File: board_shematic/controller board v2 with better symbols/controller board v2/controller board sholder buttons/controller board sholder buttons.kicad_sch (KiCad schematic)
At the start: 6 parts, among them J1 Conn_01x03_Pin, J2 Conn_01x03_Pin, SW1 SW_Push, SW2 SW_Push, SW3 SW_Push, SW4 SW_Push

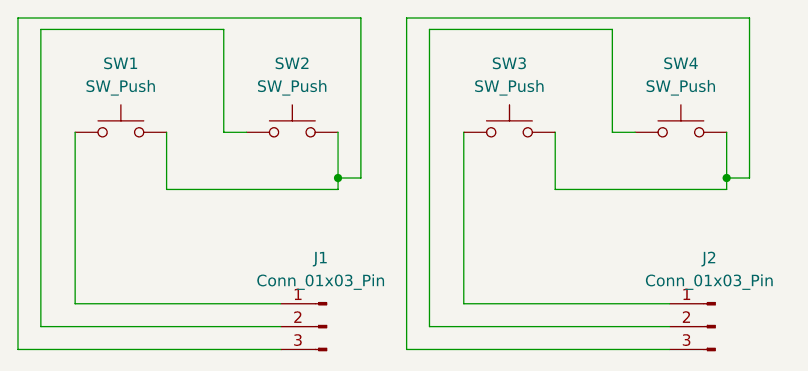
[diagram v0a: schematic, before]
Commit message: changed hole locations, updated pin orientation
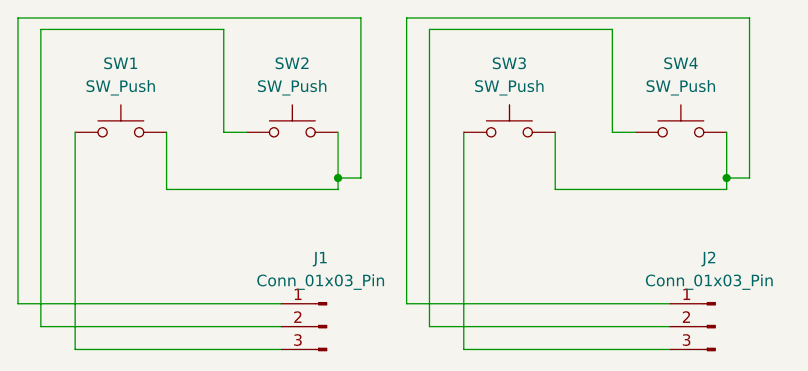
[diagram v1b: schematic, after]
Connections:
- net at J1.1 (Pin_1): now also SW1.2, SW2.2; no longer SW1.1
- net at SW3.2, SW4.2: now also J2.1 (Pin_1); no longer J2.3 (Pin_3)
- net at SW3.1: now also J2.3 (Pin_3); no longer J2.1 (Pin_1)
- new net: J1.3 (Pin_3), SW1.1
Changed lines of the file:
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@@
   (junction (at 134.62 74.93) (diameter 0) (color 0 0 0 0)
   )
+  (wire (pts (xy 134.62 74.93) (xy 137.16 74.93))
+    (stroke (width 0) (type default))
+  )
+  (wire (pts (xy 148.59 69.85) (xy 148.59 93.98))
+    (stroke (width 0) (type default))
+  )
+  (wire (pts (xy 165.1 58.42) (xy 165.1 69.85))
+    (stroke (width 0) (type default))
+  )
+  (wire (pts (xy 105.41 69.85) (xy 105.41 93.98))
+    (stroke (width 0) (type default))
+  )
+  (wire (pts (xy 142.24 57.15) (xy 142.24 88.9))
+    (stroke (width 0) (type default))
+  )
+  (wire (pts (xy 134.62 76.2) (xy 134.62 74.93))
+    (stroke (width 0) (type default))
+  )
+  (wire (pts (xy 142.24 57.15) (xy 180.34 57.15))
+    (stroke (width 0) (type default))
+  )
+  (wire (pts (xy 99.06 57.15) (xy 99.06 88.9))
+    (stroke (width 0) (type default))
+  )
+  (wire (pts (xy 177.8 74.93) (xy 177.8 69.85))
+    (stroke (width 0) (type default))
+  )
+  (wire (pts (xy 158.75 76.2) (xy 177.8 76.2))
+    (stroke (width 0) (type default))
+  )
+  (wire (pts (xy 137.16 57.15) (xy 137.16 74.93))
+    (stroke (width 0) (type default))
+  )
+  (wire (pts (xy 158.75 69.85) (xy 158.75 76.2))
+    (stroke (width 0) (type default))
+  )
+  (wire (pts (xy 99.06 57.15) (xy 137.16 57.15))
+    (stroke (width 0) (type default))
+  )
+  (wire (pts (xy 148.59 93.98) (xy 171.45 93.98))
+    (stroke (width 0) (type default))
+  )
+  (wire (pts (xy 101.6 58.42) (xy 121.92 58.42))
+    (stroke (width 0) (type default))
+  )
+  (wire (pts (xy 180.34 57.15) (xy 180.34 74.93))
+    (stroke (width 0) (type default))
+  )
+  (wire (pts (xy 171.45 91.44) (xy 144.78 91.44))
+    (stroke (width 0) (type default))
+  )
+  (wire (pts (xy 177.8 74.93) (xy 180.34 74.93))
+    (stroke (width 0) (type default))
+  )
+  (wire (pts (xy 121.92 69.85) (xy 124.46 69.85))
+    (stroke (width 0) (type default))
+  )
+  (wire (pts (xy 165.1 69.85) (xy 167.64 69.85))
+    (stroke (width 0) (type default))
+  )
   (wire (pts (xy 177.8 76.2) (xy 177.8 74.93))
     (stroke (width 0) (type default))
   )
-  (wire (pts (xy 134.62 74.93) (xy 137.16 74.93))
-    (stroke (width 0) (type default))
-  )
-  (wire (pts (xy 105.41 88.9) (xy 105.41 69.85))
-    (stroke (width 0) (type default))
-  )
-  (wire (pts (xy 171.45 91.44) (xy 144.78 91.44))
-    (stroke (width 0) (type default))
-  )
-  (wire (pts (xy 134.62 76.2) (xy 134.62 74.93))
-    (stroke (width 0) (type default))
-  )
-  (wire (pts (xy 99.06 93.98) (xy 99.06 57.15))
-    (stroke (width 0) (type default))
-  )
-  (wire (pts (xy 137.16 57.15) (xy 137.16 74.93))
-    (stroke (width 0) (type default))
-  )
-  (wire (pts (xy 177.8 74.93) (xy 177.8 69.85))
-    (stroke (width 0) (type default))
-  )
-  (wire (pts (xy 142.24 93.98) (xy 142.24 57.15))
-    (stroke (width 0) (type default))
-  )
-  (wire (pts (xy 99.06 57.15) (xy 137.16 57.15))
-    (stroke (width 0) (type default))
-  )
-  (wire (pts (xy 171.45 93.98) (xy 142.24 93.98))
-    (stroke (width 0) (type default))
-  )
-  (wire (pts (xy 101.6 58.42) (xy 121.92 58.42))
-    (stroke (width 0) (type default))
-  )
-  (wire (pts (xy 148.59 88.9) (xy 148.59 69.85))
-    (stroke (width 0) (type default))
-  )
-  (wire (pts (xy 121.92 69.85) (xy 124.46 69.85))
-    (stroke (width 0) (type default))
-  )
-  (wire (pts (xy 165.1 69.85) (xy 167.64 69.85))
-    (stroke (width 0) (type default))
-  )
-  (wire (pts (xy 165.1 58.42) (xy 165.1 69.85))
-    (stroke (width 0) (type default))
-  )
-  (wire (pts (xy 158.75 69.85) (xy 158.75 76.2))
+  (wire (pts (xy 105.41 93.98) (xy 128.27 93.98))
+    (stroke (width 0) (type default))
+  )
+  (wire (pts (xy 134.62 74.93) (xy 134.62 69.85))
+    (stroke (width 0) (type default))
+  )
+  (wire (pts (xy 128.27 91.44) (xy 101.6 91.44))
+    (stroke (width 0) (type default))
+  )
+  (wire (pts (xy 142.24 88.9) (xy 171.45 88.9))
+    (stroke (width 0) (type default))
+  )
+  (wire (pts (xy 115.57 69.85) (xy 115.57 76.2))
+    (stroke (width 0) (type default))
+  )
+  (wire (pts (xy 99.06 88.9) (xy 128.27 88.9))
+    (stroke (width 0) (type default))
+  )
+  (wire (pts (xy 101.6 91.44) (xy 101.6 58.42))
+    (stroke (width 0) (type default))
+  )
+  (wire (pts (xy 115.57 76.2) (xy 134.62 76.2))
+    (stroke (width 0) (type default))
+  )
+  (wire (pts (xy 121.92 58.42) (xy 121.92 69.85))
+    (stroke (width 0) (type default))
+  )
+  (wire (pts (xy 144.78 58.42) (xy 165.1 58.42))
     (stroke (width 0) (type default))
   )
@@
     (stroke (width 0) (type default))
   )
-  (wire (pts (xy 134.62 74.93) (xy 134.62 69.85))
-    (stroke (width 0) (type default))
-  )
-  (wire (pts (xy 128.27 91.44) (xy 101.6 91.44))
-    (stroke (width 0) (type default))
-  )
-  (wire (pts (xy 177.8 74.93) (xy 180.34 74.93))
-    (stroke (width 0) (type default))
-  )
-  (wire (pts (xy 144.78 58.42) (xy 165.1 58.42))
-    (stroke (width 0) (type default))
-  )
-  (wire (pts (xy 115.57 69.85) (xy 115.57 76.2))
-    (stroke (width 0) (type default))
-  )
-  (wire (pts (xy 142.24 57.15) (xy 180.34 57.15))
-    (stroke (width 0) (type default))
-  )
-  (wire (pts (xy 180.34 57.15) (xy 180.34 74.93))
-    (stroke (width 0) (type default))
-  )
-  (wire (pts (xy 128.27 88.9) (xy 105.41 88.9))
-    (stroke (width 0) (type default))
-  )
-  (wire (pts (xy 171.45 88.9) (xy 148.59 88.9))
-    (stroke (width 0) (type default))
-  )
-  (wire (pts (xy 101.6 91.44) (xy 101.6 58.42))
-    (stroke (width 0) (type default))
-  )
-  (wire (pts (xy 128.27 93.98) (xy 99.06 93.98))
-    (stroke (width 0) (type default))
-  )
-  (wire (pts (xy 115.57 76.2) (xy 134.62 76.2))
-    (stroke (width 0) (type default))
-  )
-  (wire (pts (xy 158.75 76.2) (xy 177.8 76.2))
-    (stroke (width 0) (type default))
-  )
-  (wire (pts (xy 121.92 58.42) (xy 121.92 69.85))
-    (stroke (width 0) (type default))
+  (symbol (lib_id "Switch:SW_Push") (at 153.67 69.85 0) (unit 1)
+    (in_bom yes) (on_board yes) (dnp no) (fields_autoplaced)
+    (property "Reference" "SW3" (at 153.67 62.23 0)
+      (effects (font (size 1.27 1.27)))
+    )
+    (property "Value" "SW_Push" (at 153.67 64.77 0)
+      (effects (font (size 1.27 1.27)))
+    )
+    (property "Footprint" "Button_Switch_THT:SW_PUSH_6mm_H5mm" (at 153.67 64.77 0)
+      (effects (font (size 1.27 1.27)) hide)
+    )
+    (property "Datasheet" "~" (at 153.67 64.77 0)
+      (effects (font (size 1.27 1.27)) hide)
+    )
+    (pin "2")
+    (pin "1")
+    (instances
+      (project "controller board sholder buttons"
+        (path "/e512c459-defe-42ca-9db2-2e1aa3ed270f"
+          (reference "SW3") (unit 1)
+        )
+      )
+    )
   )
   (symbol (lib_id "Connector:Conn_01x03_Pin") (at 133.35 91.44 0) (mirror y) (unit 1)
@@
     )
   )
-  (symbol (lib_id "Switch:SW_Push") (at 172.72 69.85 0) (unit 1)
-    (in_bom yes) (on_board yes) (dnp no) (fields_autoplaced)
-    (property "Reference" "SW4" (at 172.72 62.23 0)
-      (effects (font (size 1.27 1.27)))
-    )
-    (property "Value" "SW_Push" (at 172.72 64.77 0)
-      (effects (font (size 1.27 1.27)))
-    )
-    (property "Footprint" "Button_Switch_THT:SW_PUSH_6mm_H5mm" (at 172.72 64.77 0)
-      (effects (font (size 1.27 1.27)) hide)
-    )
-    (property "Datasheet" "~" (at 172.72 64.77 0)
-      (effects (font (size 1.27 1.27)) hide)
-    )
-    (pin "2")
-    (pin "1")
-    (instances
-      (project "controller board sholder buttons"
-        (path "/e512c459-defe-42ca-9db2-2e1aa3ed270f"
-          (reference "SW4") (unit 1)
-        )
-      )
-    )
-  )
   (symbol (lib_id "Switch:SW_Push") (at 129.54 69.85 0) (unit 1)
     (in_bom yes) (on_board yes) (dnp no) (fields_autoplaced)
@@
     )
   )
-  (symbol (lib_id "Switch:SW_Push") (at 153.67 69.85 0) (unit 1)
-    (in_bom yes) (on_board yes) (dnp no) (fields_autoplaced)
-    (property "Reference" "SW3" (at 153.67 62.23 0)
-      (effects (font (size 1.27 1.27)))
-    )
-    (property "Value" "SW_Push" (at 153.67 64.77 0)
-      (effects (font (size 1.27 1.27)))
-    )
-    (property "Footprint" "Button_Switch_THT:SW_PUSH_6mm_H5mm" (at 153.67 64.77 0)
-      (effects (font (size 1.27 1.27)) hide)
-    )
-    (property "Datasheet" "~" (at 153.67 64.77 0)
-      (effects (font (size 1.27 1.27)) hide)
-    )
-    (pin "2")
-    (pin "1")
-    (instances
-      (project "controller board sholder buttons"
-        (path "/e512c459-defe-42ca-9db2-2e1aa3ed270f"
-          (reference "SW3") (unit 1)
-        )
-      )
+  (symbol (lib_id "Switch:SW_Push") (at 172.72 69.85 0) (unit 1)
+    (in_bom yes) (on_board yes) (dnp no) (fields_autoplaced)
+    (property "Reference" "SW4" (at 172.72 62.23 0)
+      (effects (font (size 1.27 1.27)))
+    )
+    (property "Value" "SW_Push" (at 172.72 64.77 0)
+      (effects (font (size 1.27 1.27)))
+    )
+    (property "Footprint" "Button_Switch_THT:SW_PUSH_6mm_H5mm" (at 172.72 64.77 0)
+      (effects (font (size 1.27 1.27)) hide)
+    )
+    (property "Datasheet" "~" (at 172.72 64.77 0)
+      (effects (font (size 1.27 1.27)) hide)
+    )
+    (pin "2")
+    (pin "1")
+    (instances
+      (project "controller board sholder buttons"
+        (path "/e512c459-defe-42ca-9db2-2e1aa3ed270f"
+          (reference "SW4") (unit 1)
+        )
+      )
